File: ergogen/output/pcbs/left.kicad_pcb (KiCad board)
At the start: 2 copper layers, 140.9 x 96.1 mm, 85 parts

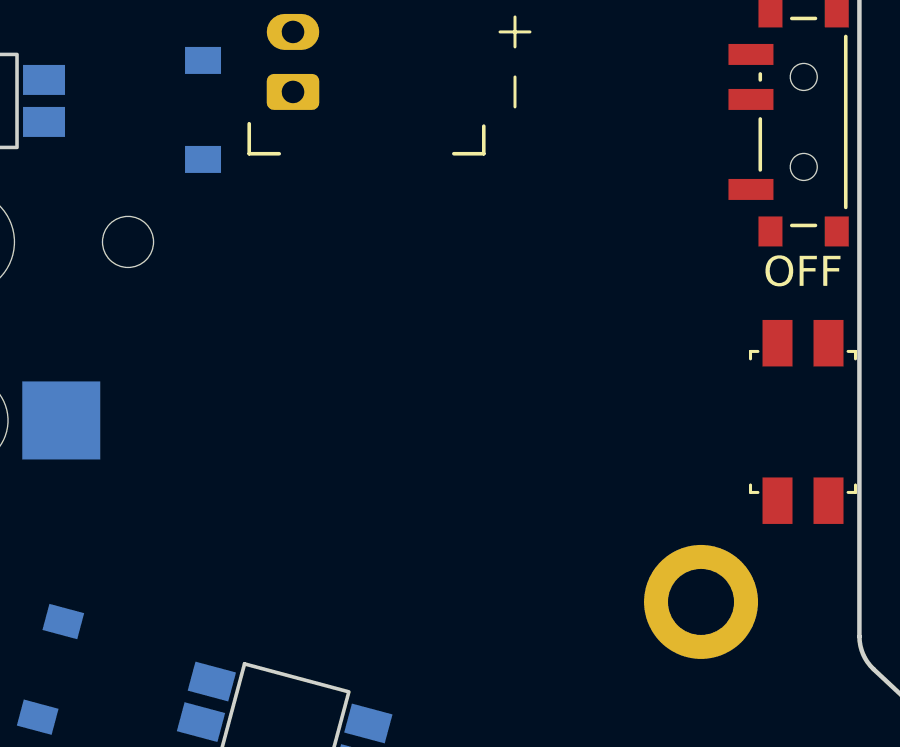
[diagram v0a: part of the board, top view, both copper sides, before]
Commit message: fix: ergogen lio logo
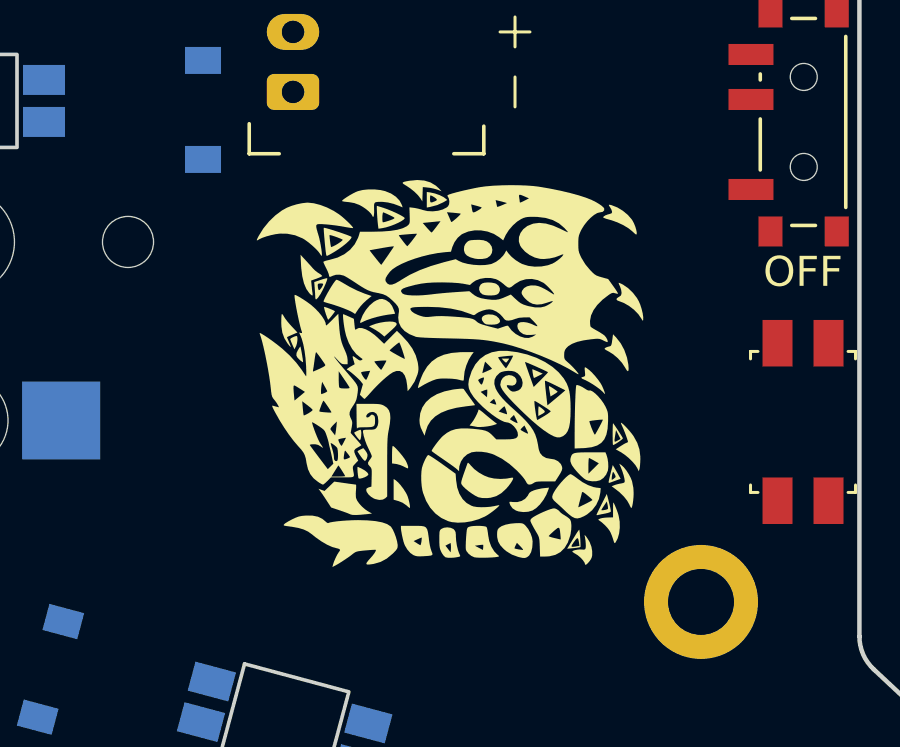
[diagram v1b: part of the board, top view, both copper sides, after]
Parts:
- added G: Lio, custom:lio, F.Cu at (156.2, 173.4)

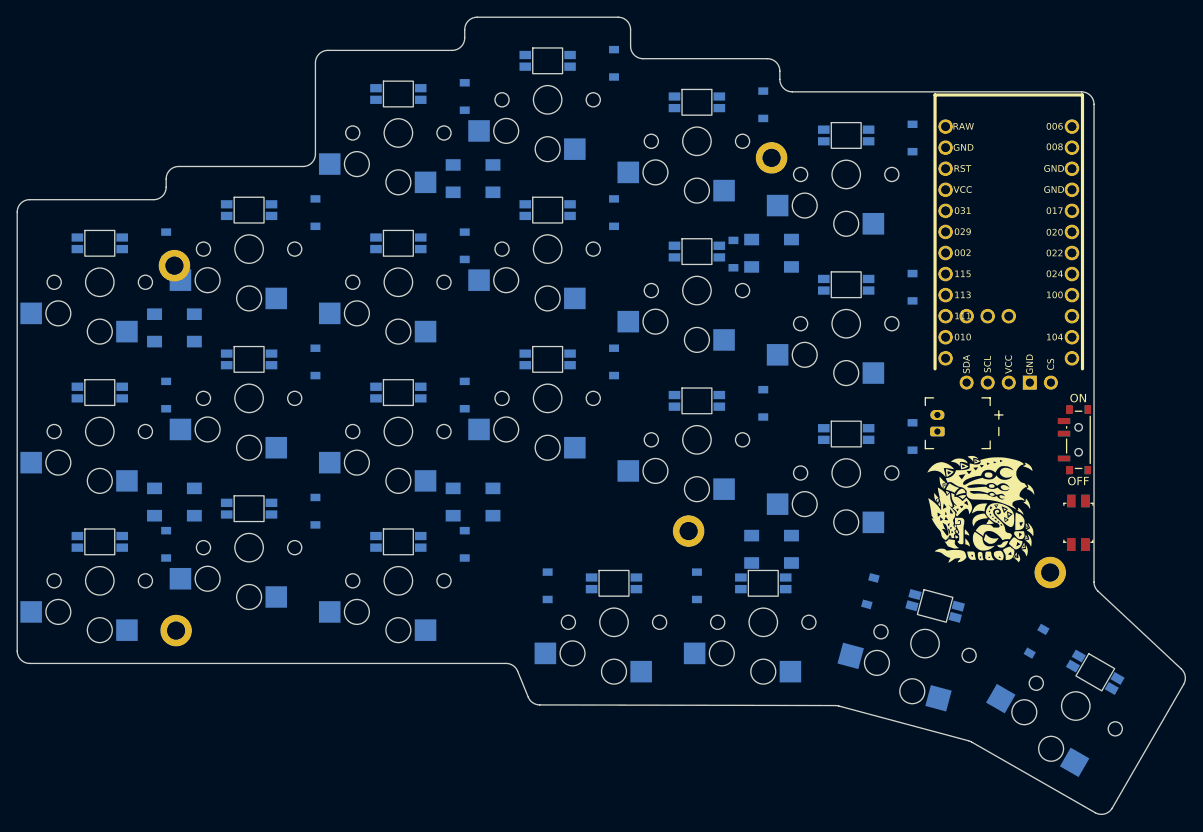
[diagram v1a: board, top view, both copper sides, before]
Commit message: add: routing paras, position adjustments
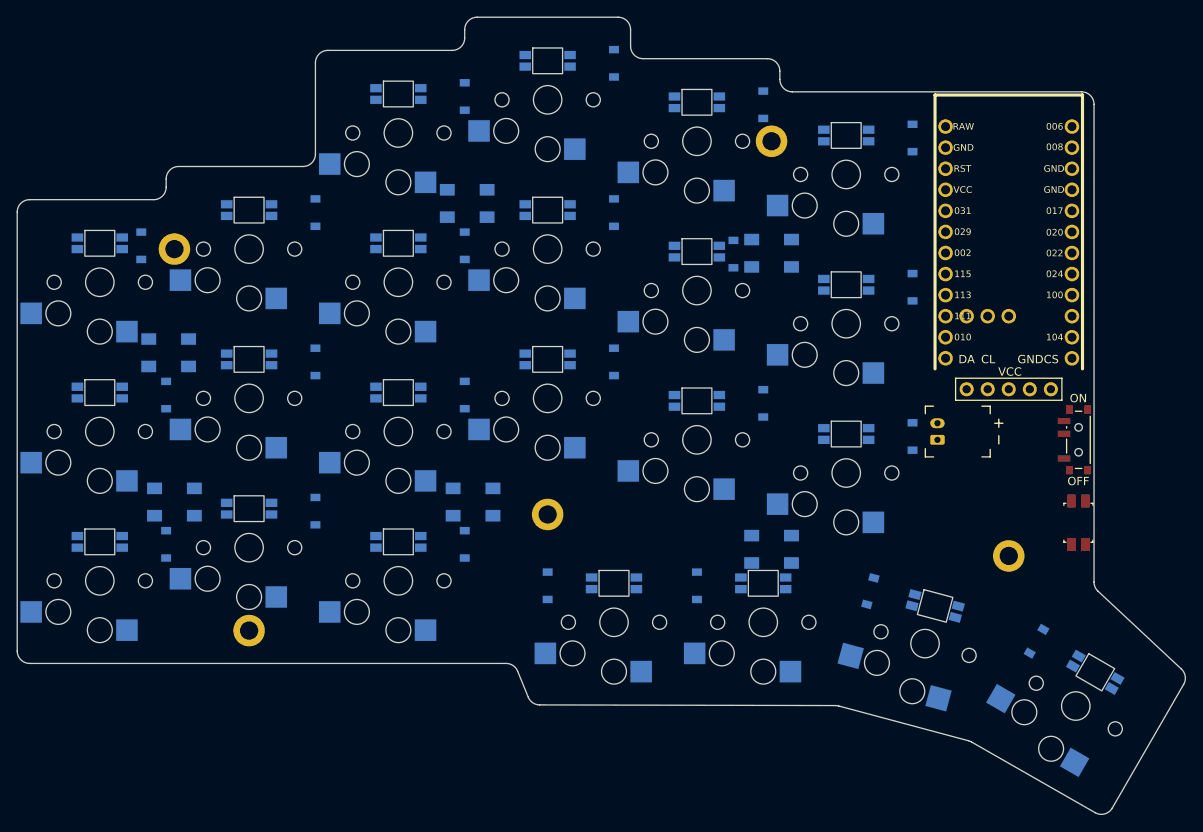
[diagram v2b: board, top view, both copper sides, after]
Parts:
- removed ?: , lib:niceView_headers
- added nice_view_headers: , ceoloide:display_nice_view, F.Cu at (159.6, 142.2)
- G: moved to B.Cu
- moved D23 71.4 mm to (55.0, 141.6)
- moved D18 69.7 mm to (104.0, 182.6)
- moved D22 59.3 mm to (126.4, 142.6), turned to 90 degrees
- moved D13 44.8 mm to (130.0, 160.6)
- moved D15 43.9 mm to (148.0, 164.6)
- moved D6 43.9 mm to (94.0, 177.6)
- moved D10 36.7 mm to (112.0, 155.6)
- moved D3 36.7 mm to (76.0, 173.6)
- moved D14 36.0 mm to (130.0, 124.6)
- moved D20 20.9 mm to (142.9, 183.2), turned to 75 degrees
- moved D21 20.9 mm to (163.0, 189.3), turned to 60 degrees
- moved D11 18.0 mm to (112.0, 137.6)
- moved D12 18.0 mm to (112.0, 119.6)
- moved D16 18.0 mm to (148.0, 146.6)
- moved D17 18.0 mm to (148.0, 128.6)
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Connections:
- D1 pad 1: (no net) -> P022
- D10 pad 1: (no net) -> P022
- D10 pad 2: ring_top -> middle_bottom
- D11 pad 1: (no net) -> P020
- D11 pad 2: middle_bottom -> middle_home
- D12 pad 1: (no net) -> P017
- D12 pad 2: middle_home -> middle_top
- D13 pad 1: (no net) -> P022
- D13 pad 2: middle_top -> index_bottom
- D14 pad 1: (no net) -> P017
- D14 pad 2: index_bottom -> index_top
- D15 pad 1: (no net) -> P022
- D15 pad 2: index_top -> inner_bottom
- D16 pad 1: (no net) -> P020
- D16 pad 2: inner_bottom -> inner_home
- D17 pad 1: (no net) -> P017
- D17 pad 2: inner_home -> inner_top
- D18 pad 1: (no net) -> P017
- D18 pad 2: inner_top -> inner_thumb
- D19 pad 1: (no net) -> P017
- D19 pad 2: inner_thumb -> close_thumb
- D2 pad 1: (no net) -> P020
- D20 pad 1: (no net) -> P017
- D20 pad 2: close_thumb -> home_thumb
- D21 pad 1: (no net) -> P017
- D21 pad 2: home_thumb -> outer_thumb
- D22 pad 1: (no net) -> P020
- D22 pad 2: outer_thumb -> index_home
- D23 pad 1: (no net) -> P017
- D23 pad 2: index_home -> outer_top
- D3 pad 1: (no net) -> P022
- D3 pad 2: outer_top -> pinky_bottom
- D4 pad 1: (no net) -> P020
- D4 pad 2: pinky_bottom -> pinky_home
- D5 pad 1: (no net) -> P017
- D5 pad 2: pinky_home -> pinky_top
- D6 pad 1: (no net) -> P024
- D6 pad 2: pinky_top -> ring_bonus
- D7 pad 1: (no net) -> P022
- D7 pad 2: ring_bonus -> ring_bottom
- D8 pad 1: (no net) -> P020
- D8 pad 2: ring_bottom -> ring_home
- D9 pad 1: (no net) -> P017
- D9 pad 2: ring_home -> ring_top
- LED1 pad 2: (no net) -> LED_23
- LED1 pad 4: (no net) -> LED_22
- LED10 pad 2: (no net) -> LED_14
- LED10 pad 4: (no net) -> LED_13
- LED11 pad 2: (no net) -> LED_11
- LED11 pad 4: (no net) -> LED_10
- LED12 pad 2: (no net) -> LED_12
- LED12 pad 4: (no net) -> LED_11
- LED13 pad 2: (no net) -> LED_13
- LED13 pad 4: (no net) -> LED_12
- LED14 pad 2: (no net) -> LED_7
- LED14 pad 4: (no net) -> LED_6
- LED15 pad 2: (no net) -> LED_6
- LED15 pad 4: (no net) -> LED_5
- LED16 pad 2: (no net) -> LED_5
- LED16 pad 4: (no net) -> LED_4
- LED17 pad 2: (no net) -> LED_2
- LED17 pad 4: (no net) -> LED_1
- LED18 pad 2: (no net) -> LED_3
- LED18 pad 4: (no net) -> LED_2
- LED19 pad 2: (no net) -> LED_4
- LED19 pad 4: (no net) -> LED_3
- LED2 pad 2: (no net) -> LED_22
- LED2 pad 4: (no net) -> LED_21
- LED20 pad 2: (no net) -> LED_10
- LED20 pad 4: (no net) -> LED_9
- LED21 pad 2: (no net) -> LED_9
- LED21 pad 4: (no net) -> LED_8
- LED22 pad 2: (no net) -> LED_8
- LED22 pad 4: (no net) -> LED_7
- LED23 pad 2: (no net) -> LED_1
- LED23 pad 4: (no net) -> ULED_6
- LED24 pad 4: LED -> P006
- LED3 pad 2: (no net) -> LED_21
- LED3 pad 4: (no net) -> LED_20
- LED4 pad 2: (no net) -> LED_18
- LED4 pad 4: (no net) -> LED_17
- LED5 pad 2: (no net) -> LED_19
- LED5 pad 4: (no net) -> LED_18
- LED6 pad 2: (no net) -> LED_20
- LED6 pad 4: (no net) -> LED_19
- LED7 pad 2: (no net) -> LED_17
- LED7 pad 4: (no net) -> LED_16
- LED8 pad 2: (no net) -> LED_16
- LED8 pad 4: (no net) -> LED_15
- LED9 pad 2: (no net) -> LED_15
- LED9 pad 4: (no net) -> LED_14
- S1 pad 1: (no net) -> P031
- S10 pad 1: (no net) -> P002
- S11 pad 1: (no net) -> P115
- S12 pad 1: (no net) -> P115
- S13 pad 1: (no net) -> P115
- S14 pad 1: (no net) -> P113
- S15 pad 1: (no net) -> P113
- S16 pad 1: (no net) -> P113
- S17 pad 1: (no net) -> P111
- S18 pad 1: (no net) -> P111
- S19 pad 1: (no net) -> P111
- S2 pad 1: (no net) -> P031
- S20 pad 1: (no net) -> P115
- S21 pad 1: (no net) -> P111
- S22 pad 1: (no net) -> P113
- S23 pad 1: (no net) -> P111
- S3 pad 1: (no net) -> P031
- S4 pad 1: (no net) -> P029
- S5 pad 1: (no net) -> P029
- S6 pad 1: (no net) -> P029
- S7 pad 1: (no net) -> P002
- S8 pad 1: (no net) -> P002
- S9 pad 1: (no net) -> P002

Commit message: update: nice_view pins
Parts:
- removed nice_view_headers: , ceoloide:display_nice_view
- added DISP1: , ceoloide:display_nice_view, F.Cu at (159.6, 142.2)
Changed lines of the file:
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@@
     (layer F.Cu)
     (at 159.6 142.2 0)
-    (property "Reference" "nice_view_headers"
+    (property "Reference" "DISP1"
       (at 0 20 0)
       (layer "F.SilkS")

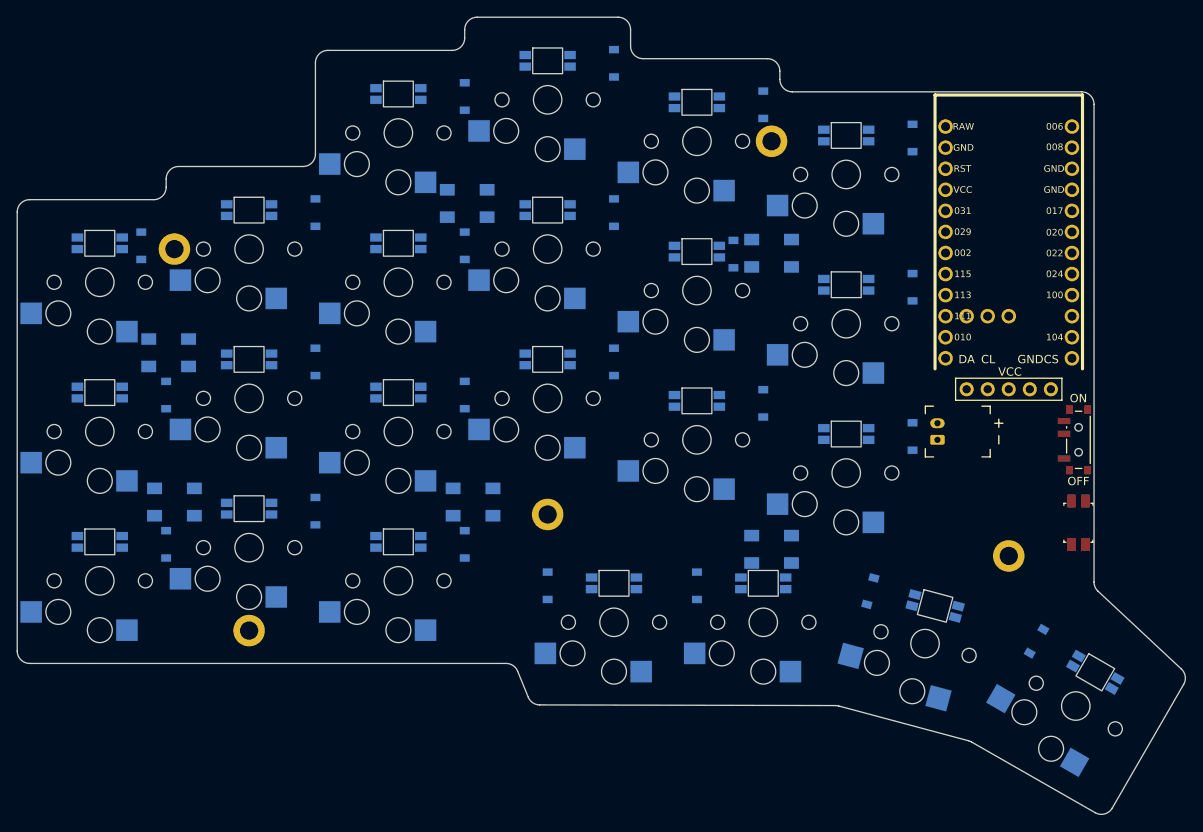
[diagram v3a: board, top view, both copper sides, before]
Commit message: fix: diode / hole / led placement
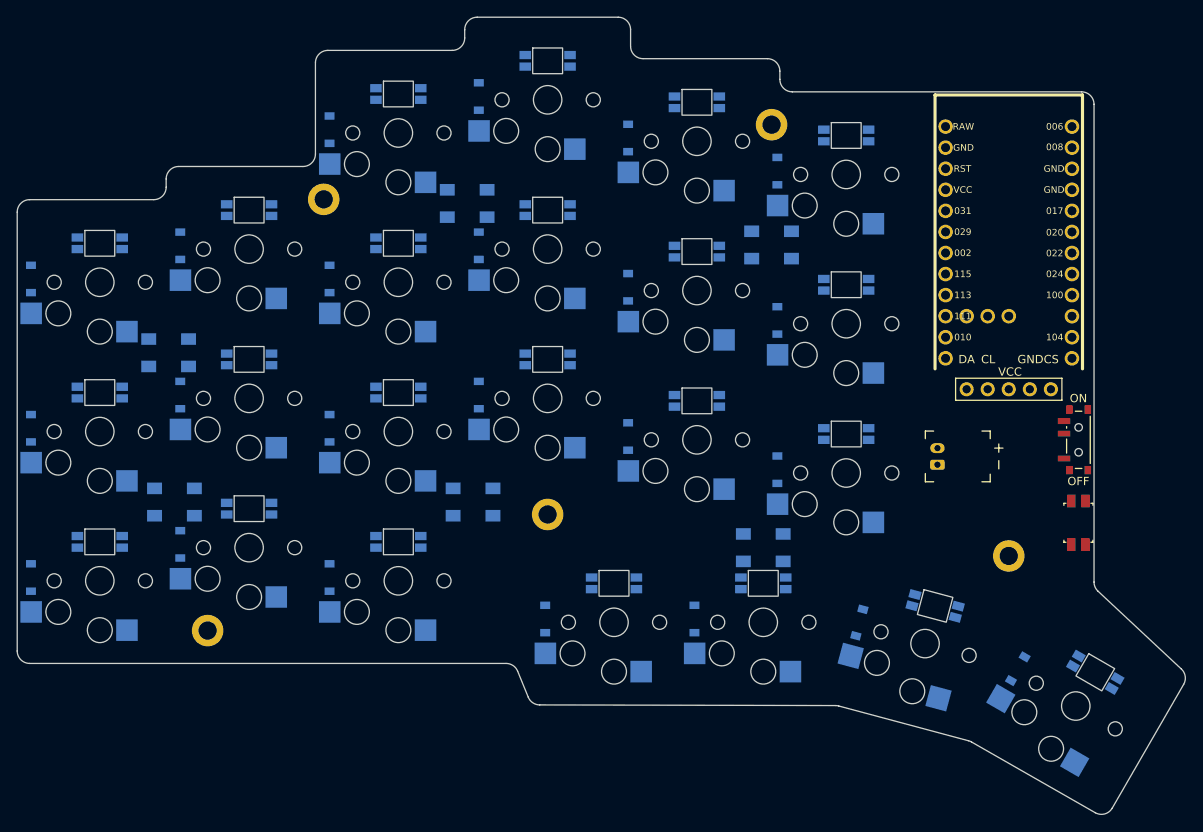
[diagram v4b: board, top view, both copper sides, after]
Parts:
- moved D23 117.4 mm to (160.7, 192.6), turned to -120 degrees
- moved D19 50.9 mm to (131.7, 132.6), turned to -90 degrees
- moved D13 50.5 mm to (95.7, 123.6), turned to -90 degrees
- moved D6 49.7 mm to (59.7, 141.6), turned to -90 degrees
- moved D22 47.0 mm to (141.6, 187.0), turned to -105 degrees
- moved D10 44.3 mm to (77.7, 127.6), turned to -90 degrees
- moved D3 44.3 mm to (41.7, 145.6), turned to -90 degrees
- moved D14 43.2 mm to (113.7, 164.6), turned to -90 degrees
- moved D17 43.2 mm to (131.7, 168.6), turned to -90 degrees
- moved D18 42.3 mm to (131.7, 150.6), turned to -90 degrees
- moved D21 41.3 mm to (121.7, 186.6), turned to -90 degrees
- moved D20 39.4 mm to (103.7, 186.6), turned to -90 degrees
- moved D15 38.7 mm to (113.7, 146.6), turned to -90 degrees
- moved D16 38.7 mm to (113.7, 128.6), turned to -90 degrees
- moved D11 27.4 mm to (95.7, 159.6), turned to -90 degrees
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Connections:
- D10 pad 1: P022 -> P017
- D10 pad 2: middle_bottom -> ring_top
- D11 pad 1: P020 -> P022
- D11 pad 2: middle_home -> middle_bottom
- D12 pad 1: P017 -> P020
- D12 pad 2: middle_top -> middle_home
- D13 pad 1: P022 -> P017
- D13 pad 2: index_bottom -> middle_top
- D14 pad 1: P017 -> P022
- D14 pad 2: index_top -> index_bottom
- D15 pad 1: P022 -> P020
- D15 pad 2: inner_bottom -> index_home
- D16 pad 1: P020 -> P017
- D16 pad 2: inner_home -> index_top
- D17 pad 1: P017 -> P022
- D17 pad 2: inner_top -> inner_bottom
- D18 pad 1: P017 -> P020
- D18 pad 2: inner_thumb -> inner_home
- D19 pad 2: close_thumb -> inner_top
- D20 pad 2: home_thumb -> inner_thumb
- D21 pad 2: outer_thumb -> close_thumb
- D22 pad 1: P020 -> P017
- D22 pad 2: index_home -> home_thumb
- D23 pad 2: outer_top -> outer_thumb
- D3 pad 1: P022 -> P017
- D3 pad 2: pinky_bottom -> outer_top
- D4 pad 1: P020 -> P022
- D4 pad 2: pinky_home -> pinky_bottom
- D5 pad 1: P017 -> P020
- D5 pad 2: pinky_top -> pinky_home
- D6 pad 1: P024 -> P017
- D6 pad 2: ring_bonus -> pinky_top
- D7 pad 1: P022 -> P024
- D7 pad 2: ring_bottom -> ring_bonus
- D8 pad 1: P020 -> P022
- D8 pad 2: ring_home -> ring_bottom
- D9 pad 1: P017 -> P020
- D9 pad 2: ring_top -> ring_home
- DISP1 pad 1: P006 -> P011
- DISP1 pad 4: P020 -> P104
- DISP1 pad 5: P017 -> P106
- LED24 pad 1: (no net) -> VCC
- LED25 pad 1: (no net) -> VCC
- LED26 pad 1: (no net) -> VCC
- LED27 pad 1: (no net) -> VCC
- LED28 pad 1: (no net) -> VCC
- LED29 pad 1: (no net) -> VCC
